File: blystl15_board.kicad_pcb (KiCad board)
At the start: 2 copper layers, 42 x 42 mm, 31 parts, among them J1 SSD1306, J5 Conn_01x03, J6 DOCK_PADS, M1 BLYSTL15, SW2 SW_Push, SW3 SW_Push, SW4 SW_Push, U1 NPM1304, U2 MAX30102EFD+T, U3 MAX30208CLB+T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

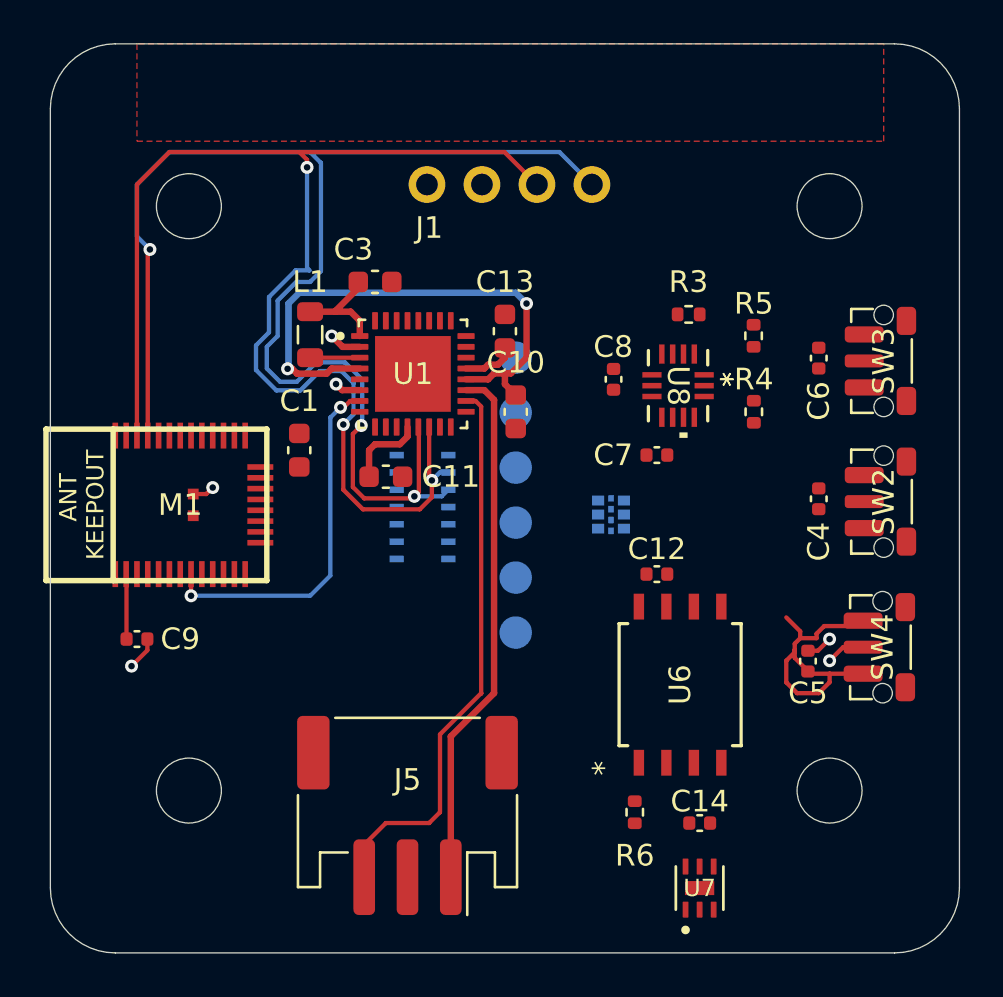
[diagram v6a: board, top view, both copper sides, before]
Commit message: Wired PMCI, dock pads, Hear Rate Sensor and 9-axis motion sensor
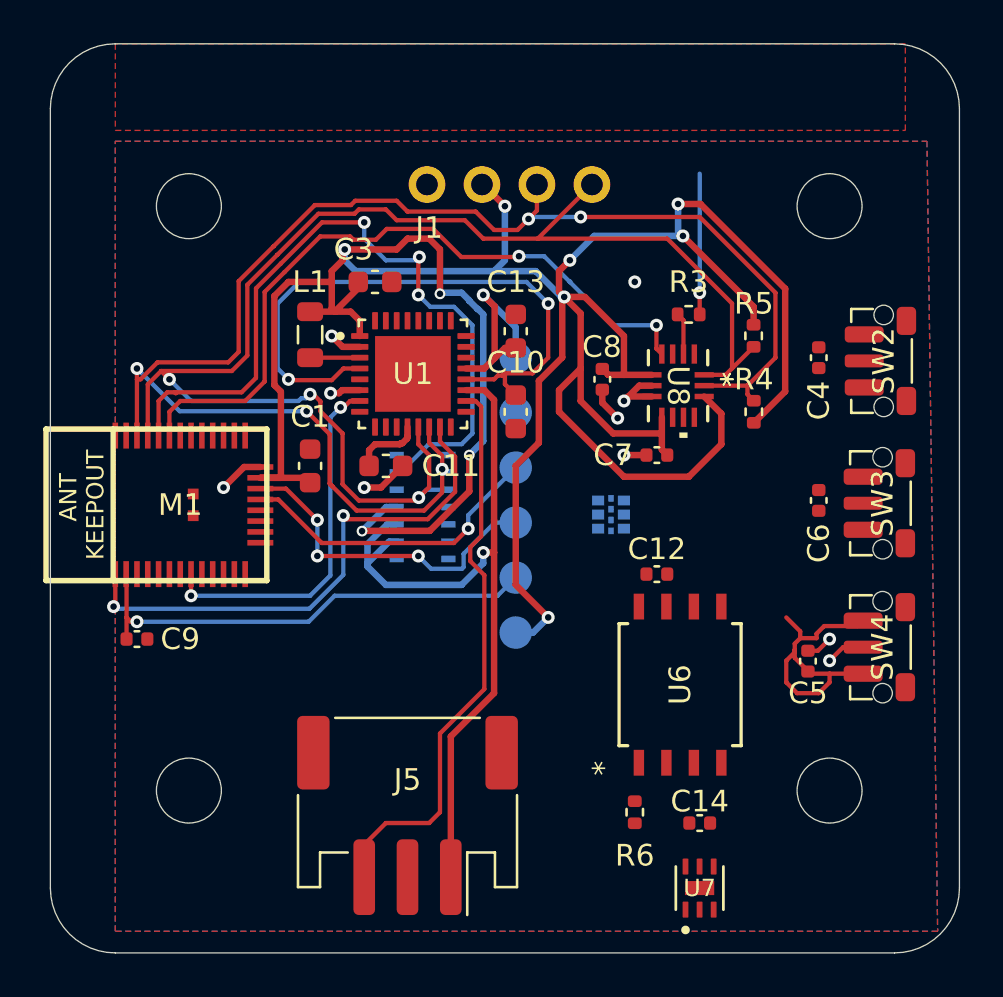
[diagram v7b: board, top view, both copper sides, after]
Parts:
- M1: value BLYSTL15 -> BLYST NANO/L15
- U1: value NPM1304 -> NPM1304-QEAA-R7
- U8: value LSM6DSV80X -> LSM6DSV80XTR
- moved SW3 6.58 mm to (169.4, 101.2)
- moved C6 6.58 mm to (166.5, 101.1)
- moved C4 6.52 mm to (166.5, 94.5)
- moved SW2 6.50 mm to (169.5, 94.7)
- moved C1 0.88 mm to (143.0, 99.5)
- moved C8 0.52 mm to (156.5, 95.5)
- moved C11 0.50 mm to (146.5, 99.5)
- moved C13 0.50 mm to (152.5, 93.3)
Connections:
- U2 pad 10: /Sensors/VBAT -> /Power Management/VBAT
- U2 pad 9: /Sensors/VBAT -> /Power Management/VBAT
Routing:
- net VDD: track 8.69 -> 147.4 mm, vias 0 -> 10
- net /P1.15: track 0.00 -> 34.8 mm, vias 0 -> 3
- net /P1.11  AIN4: track 0.00 -> 33.0 mm, vias 0 -> 2
- net /P2.09: track 0.00 -> 24.6 mm, vias 0 -> 2
- net /nRESET: track 3.01 -> 21.9 mm, vias 0 -> 1
- net /SWDCLK: track 0.00 -> 15.6 mm, vias 0 -> 3
- net /SWDIO: track 0.00 -> 14.4 mm, vias 0 -> 1
- net /Power Management/VBAT: track 24.4 -> 36.0 mm, vias 0 -> 1
- net /P1.10: track 62.5 -> 71.8 mm, vias 3 -> 5
- net GND: track 8.52 -> 16.0 mm, vias 6 -> 10
- net /Power Management/VBUS: track 2.45 -> 9.35 mm, vias 0 -> 1
- net /Sensors/QVAR_SWIPE: track 0.00 -> 6.50 mm, vias 0 -> 1
- net Net-(U1-PVDD): track 24.9 -> 28.5 mm
- net /P1.09: track 64.4 -> 67.4 mm
- net Net-(U8-SDx): track 0.00 -> 1.94 mm
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- added copper zone on B.Cu, net GND
- added copper zone on F.Cu, net GND

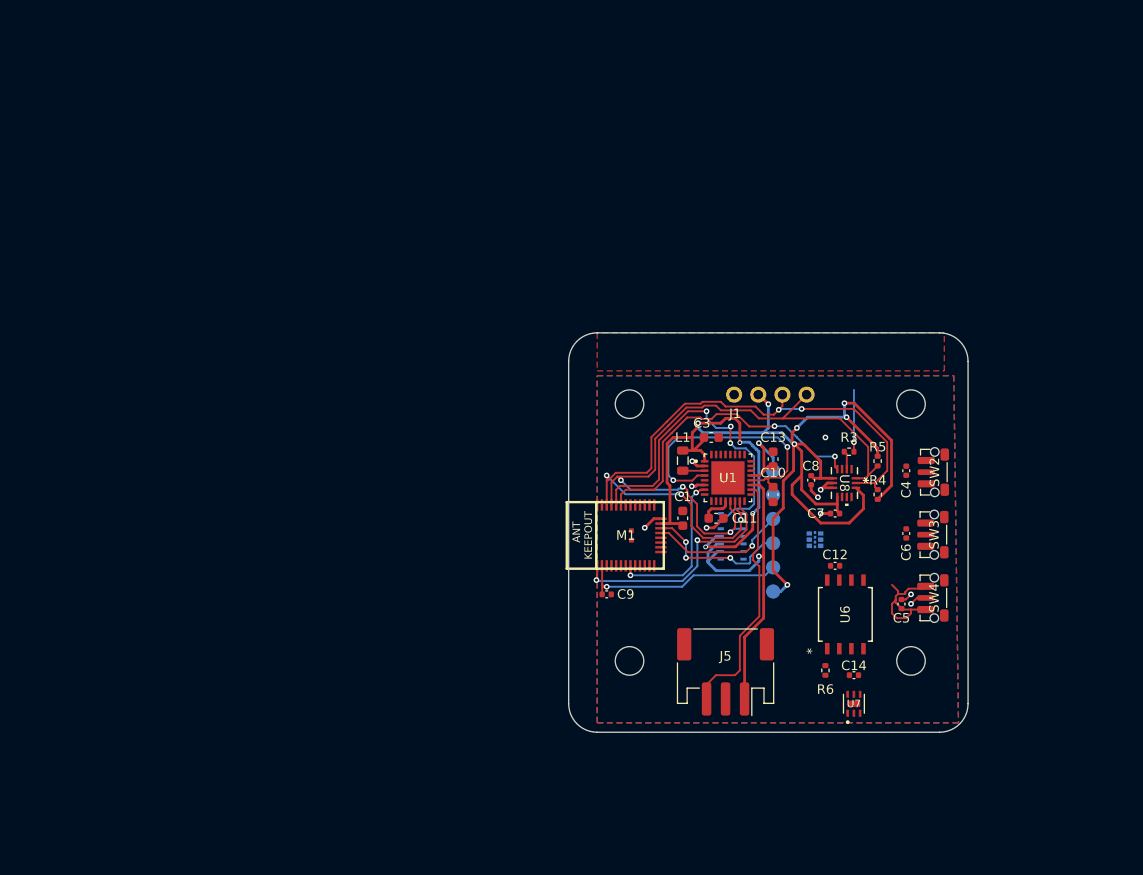
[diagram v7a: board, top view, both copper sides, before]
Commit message: Full Redesign of the Watch PCB (DRC still not fully passed)
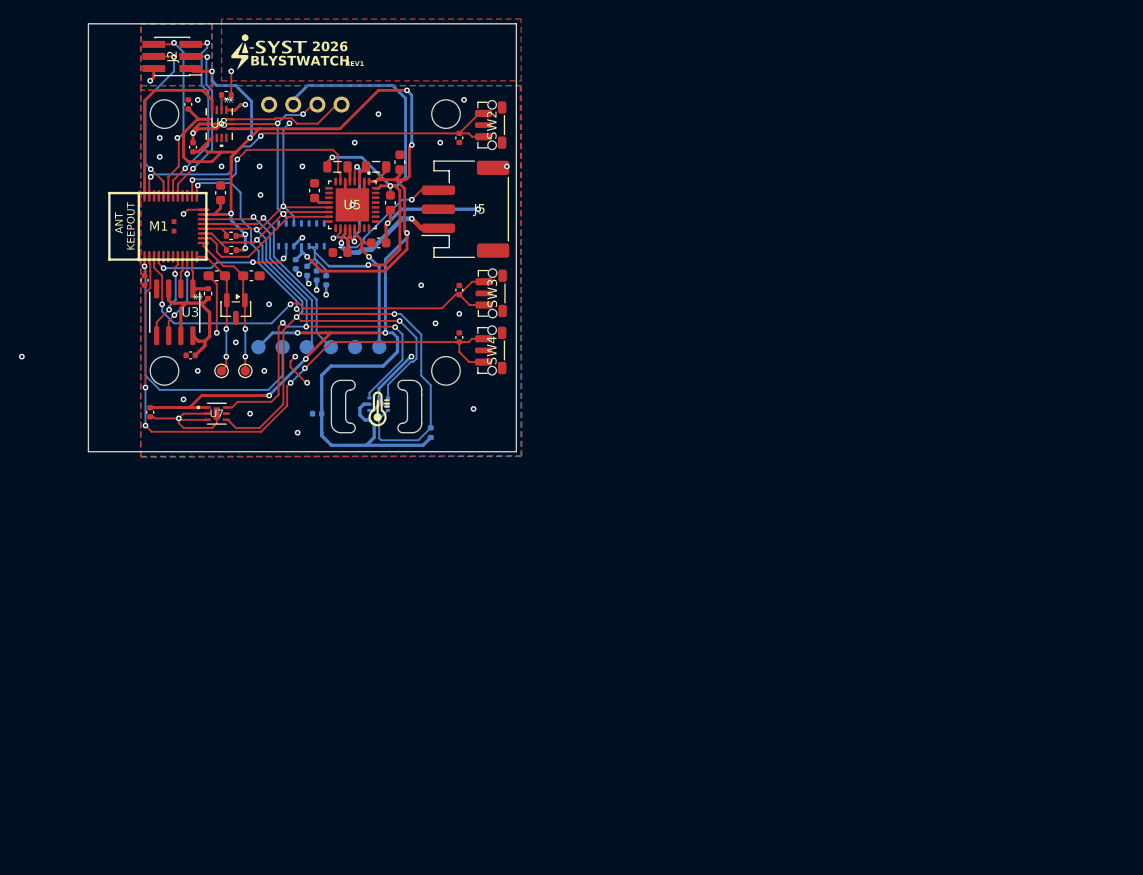
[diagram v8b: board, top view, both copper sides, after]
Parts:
- removed U1: NPM1304-QEAA-R7, 1_I_Syst.inc:QFN50P500X500X90-33N
- removed U6: W25Q80DVSSIG, 1_I_Syst.inc:WIN_SS-8_WIN-L
- added C15: 10µF, Capacitor_SMD:C_0603_1608Metric, F.Cu at (112.2, 66.3)
- added C16: C_Small, Capacitor_SMD:C_0603_1608Metric_Pad1.08x0.95mm_HandSolder, F.Cu at (97.6, 74.0)
- added C19: 0.1 μF, Capacitor_SMD:C_0402_1005Metric, B.Cu at (102.3, 72.8)
- added C2: C_Small, Capacitor_SMD:C_0603_1608Metric_Pad1.08x0.95mm_HandSolder, F.Cu at (94.0, 74.0)
- added C20: 0.1 μF, Capacitor_SMD:C_0402_1005Metric, B.Cu at (104.6, 88.5)
- added C21: 0.1 μF, Capacitor_SMD:C_0402_1005Metric, B.Cu at (103.5, 73.5)
- added C22: 4.7 μF, Capacitor_SMD:C_0402_1005Metric, B.Cu at (104.5, 74.0)
- added C23: 10 μF, Capacitor_SMD:C_0402_1005Metric, B.Cu at (105.5, 74.5)
- added D1: SP0502BAHT, Package_TO_SOT_SMD:SOT-23, F.Cu at (96.0, 77.5)
- added G***: LOGO, LOGO, F.Cu at (111.0, 88.0)
- added G***: LOGO, LOGO, F.Cu at (99.5, 50.5)
- added J2: Conn_02x03_Odd_Even, Connector_PinHeader_1.27mm:PinHeader_2x03_P1.27mm_Vertical_SMD, F.Cu at (89.3, 50.9)
- added L2: 1.0µH, Inductor_SMD:L_0805_2012Metric, F.Cu at (106.7, 62.5)
- added R9: 5kΩ, Resistor_SMD:R_0402_1005Metric, B.Cu at (116.5, 90.5)
- added TP2: TestPoint, TestPoint:TestPoint_Pad_D1.0mm, F.Cu at (97.0, 84.0)
- added TP3: TestPoint, TestPoint:TestPoint_Pad_D1.0mm, F.Cu at (94.5, 84.0)
- added U4: TMP117AIDRVT, 1_I_Syst.inc:DRV0006B, B.Cu at (111.0, 87.5)
- added U5: NPM1304-QEAA-R7, 1_I_Syst.inc:QFN50P500X500X90-33N, F.Cu at (108.2, 66.5)
- U3: value MAX30208CLB+T -> W25Q80EWSNIG; footprint 1_I_Syst.inc:21-100265_MXM -> 1_I_Syst.inc:W25Q80EWSNIG_WIN-M; moved to F.Cu
- moved C14 79.0 mm to (87.0, 88.3), turned to -90 degrees
- moved C7 77.7 mm to (91.5, 60.5), turned to -90 degrees
- moved C8 76.5 mm to (91.0, 56.0), turned to -90 degrees
- moved R6 76.1 mm to (93.1, 75.9)
- moved U8 75.8 mm to (94.2, 58.0)
- moved R3 75.5 mm to (95.0, 55.0)
- moved U7 73.6 mm to (94.0, 88.5), turned to 0 degrees
- moved R4 73.2 mm to (95.5, 69.8), turned to 180 degrees
- moved R5 71.5 mm to (95.5, 71.3), turned to 180 degrees
- moved U3 71.4 mm to (89.6, 77.8), turned to -90 degrees
- moved C12 71.3 mm to (91.2, 82.4), turned to 180 degrees
- moved C1 59.4 mm to (94.4, 65.3)
- moved SW2 59.2 mm to (123.0, 58.1)
- moved C9 58.8 mm to (86.4, 74.5), turned to -90 degrees
- moved C4 58.6 mm to (119.5, 59.5)
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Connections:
- C4 pad 2: /P1.08 -> /P1.10
- C6 pad 1: /P2.00 -> /P0.01  TXD
- J1 pad 2: VDD -> VDD_3V3
- J1 pad 3: /P1.10 -> /P2.02
- J1 pad 4: /P1.09 -> /P1.08
- R4 pad 2: /P1.10 -> /P1.08
- R5 pad 2: /P1.09 -> /P2.02
- R6 pad 2: /P2.04 -> /P2.00
- SW2 pad 1: /P1.08 -> /P1.10
- SW3 pad 1: /P2.00 -> /P0.01  TXD
- U2 pad 10: /Power Management/VBAT -> VDD_3V3
- U2 pad 13: /P1.15 -> /P0.00  RXD
- U2 pad 2: /P1.10 -> /P2.02
- U2 pad 3: /P1.09 -> /P1.08
- U2 pad 9: /Power Management/VBAT -> VDD_3V3
- U3 pad 1: VDD -> /P2.00
- U3 pad 2: VDD -> /P2.05
- U3 pad 5: GND -> /P2.04
- U3 pad 6: GND -> /P2.03
- U3 pad 7: /P2.03 -> VDD
- U3 pad 8: /P1.09 -> VDD
- U7 pad 4: /P1.10 -> /P2.02
- U7 pad 6: /P1.09 -> /P1.08
- U8 pad 13: /P1.10 -> /P2.02
- U8 pad 14: /P1.09 -> /P1.08
- U8 pad 4: /P1.11  AIN4 -> /P0.04  RTS
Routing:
- net /P1.08: track 0.00 -> 86.9 mm, vias 0 -> 6
- net /P2.02: track 0.00 -> 86.0 mm, vias 0 -> 7
- net VDD: track 147.4 -> 218.4 mm, vias 10 -> 13
- net /P1.09: track 67.4 -> 0.00 mm, vias 3 -> 0
- net VDD_3V3: track 0.00 -> 58.8 mm, vias 0 -> 3
- net GND: track 16.0 -> 73.0 mm, vias 10 -> 41
- net /P1.07  AIN3: track 0.00 -> 54.6 mm, vias 0 -> 3
- net /P0.03: track 13.6 -> 63.2 mm, vias 0 -> 4
- net /P0.01  TXD: track 0.00 -> 45.7 mm, vias 0 -> 2
- net /P1.15: track 34.8 -> 0.00 mm, vias 3 -> 0
- net /P1.10: track 71.8 -> 43.3 mm, vias 5 -> 2
- net /P2.09: track 24.6 -> 0.00 mm, vias 2 -> 0
- net /P1.06  AIN2: track 0.00 -> 22.2 mm, vias 0 -> 2
- net /Power Management/VBAT: track 36.0 -> 14.4 mm, vias 1 -> 2
- net /P1.13  AIN6: track 0.00 -> 20.0 mm, vias 0 -> 2
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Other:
- board size 42 x 42 mm -> 45 x 45 mm
- board text added: "2026"
- board text added: "BLYSTWATCH"
- board text added: "REV1"
